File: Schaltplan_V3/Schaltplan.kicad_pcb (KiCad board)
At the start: 2 copper layers, 37.8 x 37.8 mm, 13 parts, among them IC1 STM32G031J6M6, J1 Conn_01x01, J2 Conn_01x04_Male, U1 HU2032-LF

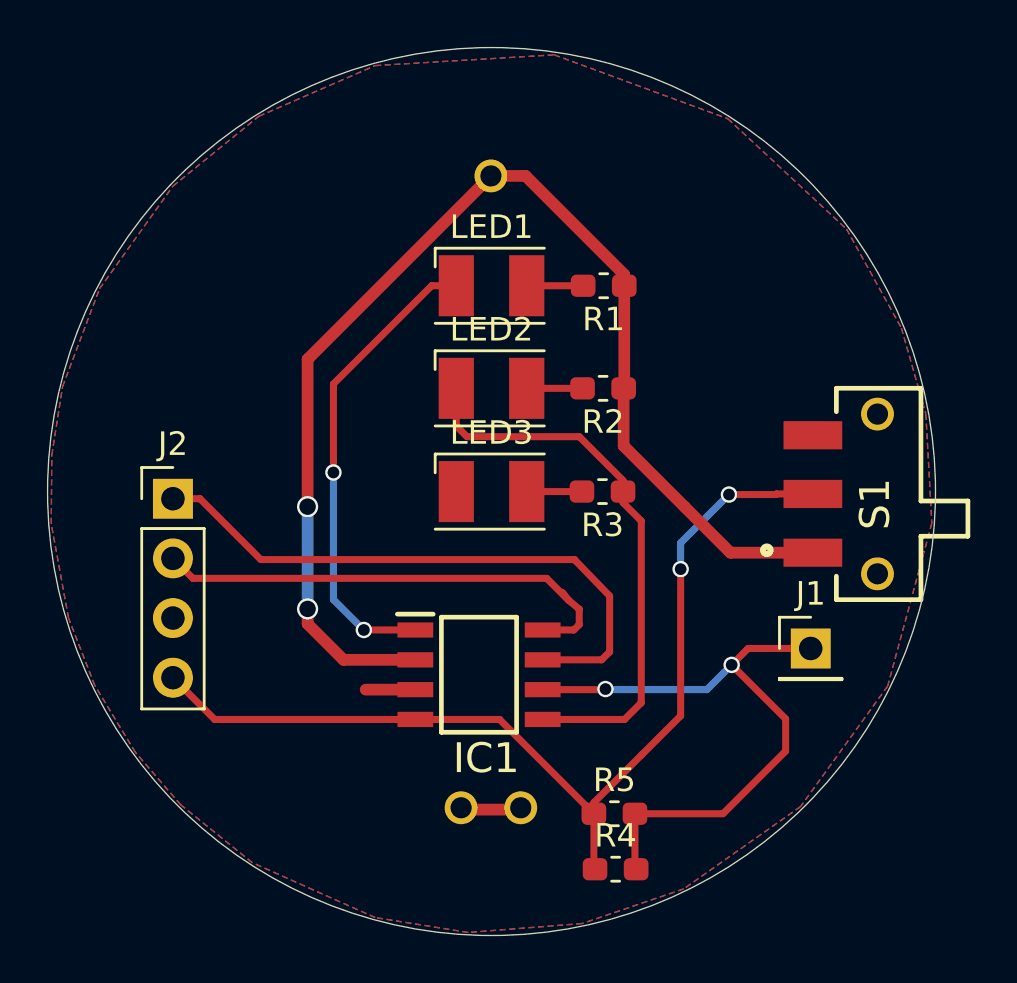
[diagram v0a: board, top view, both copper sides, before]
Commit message: Sensorpads hinzugefügt
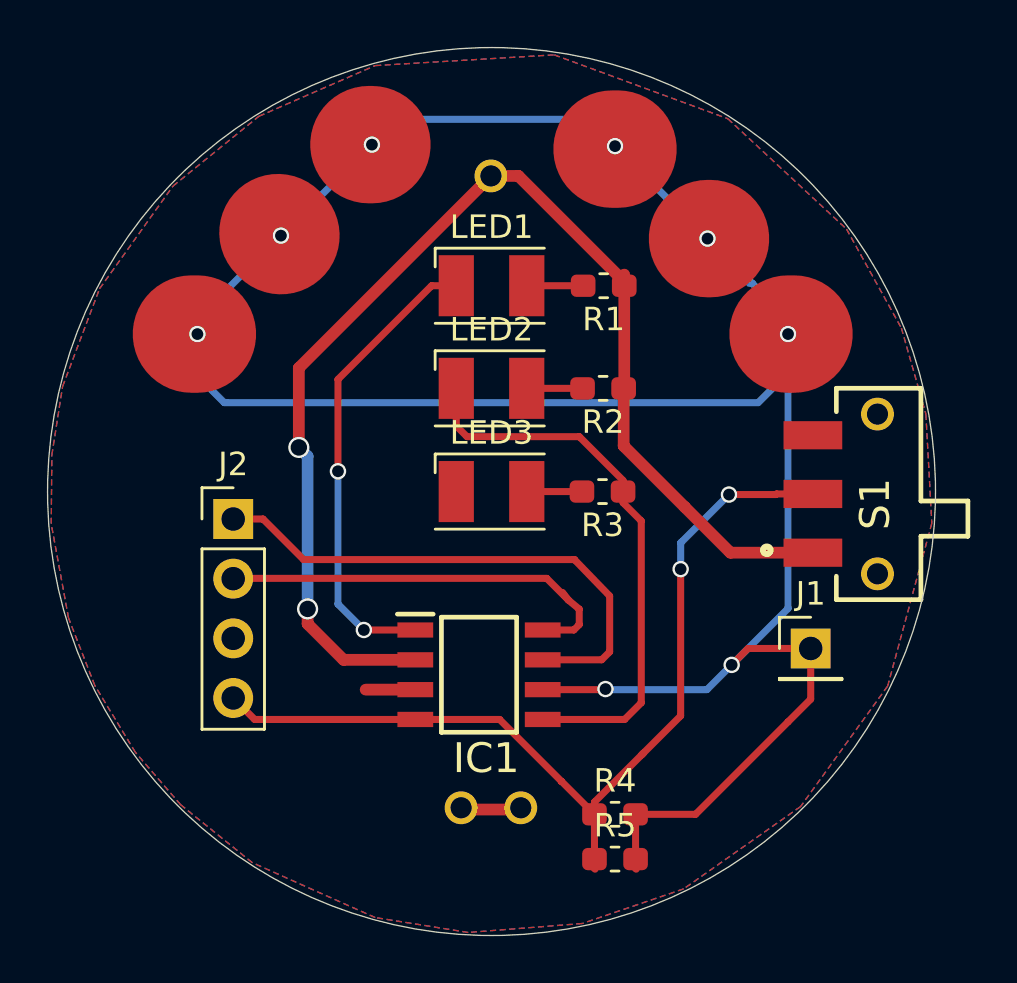
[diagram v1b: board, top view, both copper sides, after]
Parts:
- moved J2 2.71 mm to (133.2, 117.5)
- moved R4 2.34 mm to (149.5, 130.0)
- moved R5 1.93 mm to (149.5, 132.0)
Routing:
- net PA12ReceivePin-kS: track 26.7 -> 104.5 mm, vias 2 -> 8
- net Conn-RST: track 42.3 -> 39.1 mm
- net Conn-SWDIO: track 25.7 -> 22.8 mm
- net Conn-SWCLK: track 20.9 -> 18.0 mm
- net +3V3: track 52.2 -> 52.8 mm
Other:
- net class X added: clearance 0.7, trace_width 0.3, via_dia 0.7, via_drill 0.5

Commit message: mit Sensor, Platine fertig
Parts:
- removed S1: JS102011SAQN, JS102011SAQN:JS102011SAQN
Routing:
- net PA12ReceivePin-kS: track 104.5 -> 76.5 mm
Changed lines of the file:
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@@
-(kicad_pcb (version 20171130) (host pcbnew "(5.1.6)-1")
+(kicad_pcb (version 20171130) (host pcbnew "(5.1.5)-3")
   (general
     (thickness 1.6)
     (drawings 1)
-    (tracks 137)
+    (tracks 130)
     (zones 0)
-    (modules 13)
-    (nets 13)
+    (modules 12)
+    (nets 12)
   )
   (page A4)
@@
     (aux_axis_origin 0 0)
     (grid_origin 156.845 111.379)
-    (visible_elements 7FFFFFFF)
+    (visible_elements 7FFDFF7F)
     (pcbplotparams
       (layerselection 0x010fc_ffffffff)
@@
   (net 10 "Net-(LED2-Pad2)")
   (net 11 "Net-(LED3-Pad2)")
-  (net 12 "Net-(S1-Pad3)")
   (net_class Default "Dies ist die voreingestellte Netzklasse."
     (clearance 0.3)
@@
     (add_net "Net-(LED2-Pad2)")
     (add_net "Net-(LED3-Pad2)")
-    (add_net "Net-(S1-Pad3)")
     (add_net PA8-LEDs)
     (add_net PB7-LEDs)
@@
     (tags "LED PLCC-2 SMD")
     (attr smd)
-    (fp_text reference LED2 (at 0 -2.5) (layer F.SilkS)
+    (fp_text reference LED2 (at -4.5452 0) (layer F.SilkS)
       (effects (font (size 1 1) (thickness 0.15)))
     )
@@
     (tags "LED PLCC-2 SMD")
     (attr smd)
-    (fp_text reference LED3 (at 0 -2.5) (layer F.SilkS)
+    (fp_text reference LED3 (at -0.0508 2.5654) (layer F.SilkS)
       (effects (font (size 1 1) (thickness 0.15)))
     )
@@
     (tags "resistor handsolder")
     (attr smd)
-    (fp_text reference R4 (at 0 -1.43) (layer F.SilkS)
+    (fp_text reference R4 (at -0.0254 -1.4224) (layer F.SilkS)
       (effects (font (size 1 1) (thickness 0.15)))
     )
@@
     (tags "resistor handsolder")
     (attr smd)
-    (fp_text reference R5 (at 0 -1.43) (layer F.SilkS)
+    (fp_text reference R5 (at -0.5842 1.5494) (layer F.SilkS)
       (effects (font (size 1 1) (thickness 0.15)))
     )
@@
     )
   )
-  (module JS102011SAQN:JS102011SAQN (layer F.Cu)
-    (at 158.9024 116.4082 90)
-    (descr JS102011SAQN)
-    (tags Switch)
-    (fp_text reference S1 (at -0.43 1.647 90) (layer F.SilkS)
-      (effects (font (size 1.27 1.27) (thickness 0.254)))
-    )
-    (fp_text value JS102011SAQN (at -0.43 1.647 90) (layer F.SilkS) hide
-      (effects (font (size 1.27 1.27) (thickness 0.254)))
-    )
-    (fp_circle (center -2.399 -2.96) (end -2.56315 -2.96) (layer F.SilkS) (width 0.254))
-    (fp_line (start 4.5 3.6) (end 4.5 0) (layer F.SilkS) (width 0.2))
-    (fp_line (start -0.3 3.6) (end 4.5 3.6) (layer F.SilkS) (width 0.2))
-    (fp_line (start -0.3 5.6) (end -0.3 3.6) (layer F.SilkS) (width 0.2))
-    (fp_line (start -1.8 5.6) (end -0.3 5.6) (layer F.SilkS) (width 0.2))
-    (fp_line (start -1.8 3.6) (end -1.8 5.6) (layer F.SilkS) (width 0.2))
-    (fp_line (start -4.5 3.6) (end -1.8 3.6) (layer F.SilkS) (width 0.2))
-    (fp_line (start -4.5 0) (end -4.5 3.6) (layer F.SilkS) (width 0.2))
-    (fp_line (start -0.3 5.6) (end -0.3 3.6) (layer Dwgs.User) (width 0.2))
-    (fp_line (start -1.8 5.6) (end -0.3 5.6) (layer Dwgs.User) (width 0.2))
-    (fp_line (start -1.8 3.6) (end -1.8 5.6) (layer Dwgs.User) (width 0.2))
-    (fp_line (start -4.5 0) (end -3.5 0) (layer F.SilkS) (width 0.2))
-    (fp_line (start 4.5 0) (end 3.5 0) (layer F.SilkS) (width 0.2))
-    (fp_line (start -4.5 3.6) (end -4.5 0) (layer Dwgs.User) (width 0.2))
-    (fp_line (start 4.5 3.6) (end -4.5 3.6) (layer Dwgs.User) (width 0.2))
-    (fp_line (start 4.5 0) (end 4.5 3.6) (layer Dwgs.User) (width 0.2))
-    (fp_line (start -4.5 0) (end 4.5 0) (layer Dwgs.User) (width 0.2))
-    (pad 1 smd rect (at -2.5 -1 90) (size 1.2 2.5) (layers F.Cu F.Paste F.Mask)
-      (net 2 +3V3))
-    (pad 2 smd rect (at 0 -1 90) (size 1.2 2.5) (layers F.Cu F.Paste F.Mask)
-      (net 4 Conn-RST))
-    (pad 3 smd rect (at 2.5 -1 90) (size 1.2 2.5) (layers F.Cu F.Paste F.Mask)
-      (net 12 "Net-(S1-Pad3)"))
-    (pad 4 thru_hole circle (at -3.4 1.75 180) (size 1.4 1.4) (drill 0.9) (layers *.Cu *.Mask F.SilkS))
-    (pad 5 thru_hole circle (at 3.4 1.75 180) (size 1.4 1.4) (drill 0.9) (layers *.Cu *.Mask F.SilkS))
-  )
   (gr_circle (center 144.2212 116.304918) (end 161.417 108.458) (layer Edge.Cuts) (width 0.05))
   (via (at 138.7856 122.1994) (size 0.7) (drill 0.5) (layers F.Cu B.Cu) (net 1))
@@
   (segment (start 141.6712 107.5436) (end 137.683056 111.531744) (width 0.3) (layer F.Cu) (net 1))
   (segment (start 137.683056 111.531744) (end 137.683056 115.4416) (width 0.3) (layer F.Cu) (net 1))
-  (segment (start 149.8714 107.0686) (end 149.8714 107.5436) (width 0.5) (layer F.Cu) (net 2))
   (segment (start 136.390199 121.302599) (end 136.390199 121.302599) (width 0.5) (layer B.Cu) (net 2))
   (via (at 136.390199 121.302599) (size 0.9) (drill 0.7) (layers F.Cu B.Cu) (net 2))
@@
   (via (at 136.017002 114.426998) (size 0.9) (drill 0.7) (layers F.Cu B.Cu) (net 2))
   (segment (start 144.1958 102.8686) (end 136.017002 111.047398) (width 0.5) (layer F.Cu) (net 2))
-  (segment (start 145.367952 102.8686) (end 144.1958 102.8686) (width 0.5) (layer F.Cu) (net 2))
-  (segment (start 149.8714 107.372048) (end 145.367952 102.8686) (width 0.5) (layer F.Cu) (net 2))
-  (segment (start 149.8714 107.5436) (end 149.8714 107.372048) (width 0.5) (layer F.Cu) (net 2))
+  (segment (start 149.8714 107.0686) (end 149.8714 107.5436) (width 0.5) (layer F.Cu) (net 2))
+  (segment (start 149.12139 106.31859) (end 149.8714 107.0686) (width 0.5) (layer F.Cu) (net 2))
+  (segment (start 147.64579 106.31859) (end 149.12139 106.31859) (width 0.5) (layer F.Cu) (net 2))
+  (segment (start 144.1958 102.8686) (end 147.64579 106.31859) (width 0.5) (layer F.Cu) (net 2))
   (segment (start 145.3896 129.8448) (end 142.8496 129.8448) (width 0.5) (layer F.Cu) (net 3) (status 30))
   (segment (start 138.8618 124.7394) (end 140.9758 124.7394) (width 0.5) (layer F.Cu) (net 3))
-  (segment (start 148.5786 132.334) (end 148.6294 132.3848) (width 0.3) (layer F.Cu) (net 4))
   (segment (start 150.6182 127.508) (end 150.622 127.508) (width 0.3) (layer F.Cu) (net 4))
   (segment (start 140.9758 126.0094) (end 144.5654 126.0094) (width 0.3) (layer F.Cu) (net 4))
@@
   (segment (start 155.1432 122.9868) (end 154.4447 123.6853) (width 0.3) (layer F.Cu) (net 8))
   (segment (start 157.8102 122.9868) (end 155.1432 122.9868) (width 0.3) (layer F.Cu) (net 8))
-  (segment (start 150.3286 132.334) (end 150.3794 132.3848) (width 0.3) (layer F.Cu) (net 8))
   (segment (start 154.4447 123.6853) (end 156.845 121.285) (width 0.3) (layer B.Cu) (net 8))
   (segment (start 148.336 100.457) (end 148.336 100.457) (width 0.3) (layer B.Cu) (net 8))
@@
   (segment (start 156.845 108.966) (end 155.321 107.442) (width 0.3) (layer B.Cu) (net 8))
   (segment (start 156.845 108.966) (end 156.845 108.966) (width 0.3) (layer B.Cu) (net 8))
-  (via (at 156.845 109.601) (size 0.7) (drill 0.5) (layers F.Cu B.Cu) (net 8))
+  (via (at 156.845 109.0422) (size 0.7) (drill 0.5) (layers F.Cu B.Cu) (net 8))
   (via (at 149.479 101.6) (size 0.7) (drill 0.5) (layers F.Cu B.Cu) (net 8))
   (segment (start 150.3286 130.0226) (end 150.6474 130.0226) (width 0.3) (layer F.Cu) (net 8))
@@
   (segment (start 156.845 126.111) (end 157.8102 125.1458) (width 0.3) (layer F.Cu) (net 8))
   (segment (start 150.354 130.048) (end 150.354 131.953) (width 0.3) (layer F.Cu) (net 8))
-  (segment (start 156.845 111.252) (end 156.845 108.966) (width 0.3) (layer B.Cu) (net 8))
-  (segment (start 156.845 121.285) (end 156.845 111.252) (width 0.3) (layer B.Cu) (net 8))
   (segment (start 140.589 100.457) (end 140.589 100.457) (width 0.3) (layer B.Cu) (net 8))
-  (segment (start 155.575 112.522) (end 156.845 111.252) (width 0.3) (layer B.Cu) (net 8))
-  (segment (start 132.969 112.522) (end 155.575 112.522) (width 0.3) (layer B.Cu) (net 8))
-  (segment (start 132.842 112.522) (end 132.969 112.522) (width 0.3) (layer B.Cu) (net 8))
-  (segment (start 131.699 111.379) (end 132.842 112.522) (width 0.3) (layer B.Cu) (net 8))
   (segment (start 131.699 109.347) (end 131.699 109.601) (width 0.3) (layer B.Cu) (net 8))
   (segment (start 149.5425 101.6635) (end 148.336 100.457) (width 0.3) (layer B.Cu) (net 8))
-  (segment (start 131.699 109.601) (end 131.699 111.379) (width 0.3) (layer B.Cu) (net 8))
   (via (at 131.699 109.601) (size 0.7) (drill 0.5) (layers F.Cu B.Cu) (net 8))
   (segment (start 148.336 100.457) (end 140.208 100.457) (width 0.3) (layer B.Cu) (net 8))
@@
   (segment (start 149.606 101.727) (end 149.352 101.727) (width 5) (layer F.Cu) (net 8))
   (segment (start 139.0015 101.5365) (end 139.1285 101.5365) (width 5) (layer F.Cu) (net 8))
+  (segment (start 156.845 108.966) (end 156.845 109.601) (width 0.3) (layer B.Cu) (net 8))
+  (segment (start 156.845 121.285) (end 156.845 109.601) (width 0.3) (layer B.Cu) (net 8))
   (segment (start 148.1214 107.5436) (end 145.7212 107.5436) (width 0.3) (layer F.Cu) (net 9))
   (segment (start 148.096 111.9124) (end 145.7198 111.9124) (width 0.3) (layer F.Cu) (net 10))
